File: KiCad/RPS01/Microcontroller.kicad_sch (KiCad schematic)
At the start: 20 parts, among them J1 Conn_02x03_Counter_Clockwise, J2 Conn_01x06, J3 Conn_01x03, J4 Conn_01x02_Pin, J5 XT30, J6 AandDpin, J7 Conn_01x03, SW1 MCU_Button, U1 ATmega328P-A, U2 AMS1117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

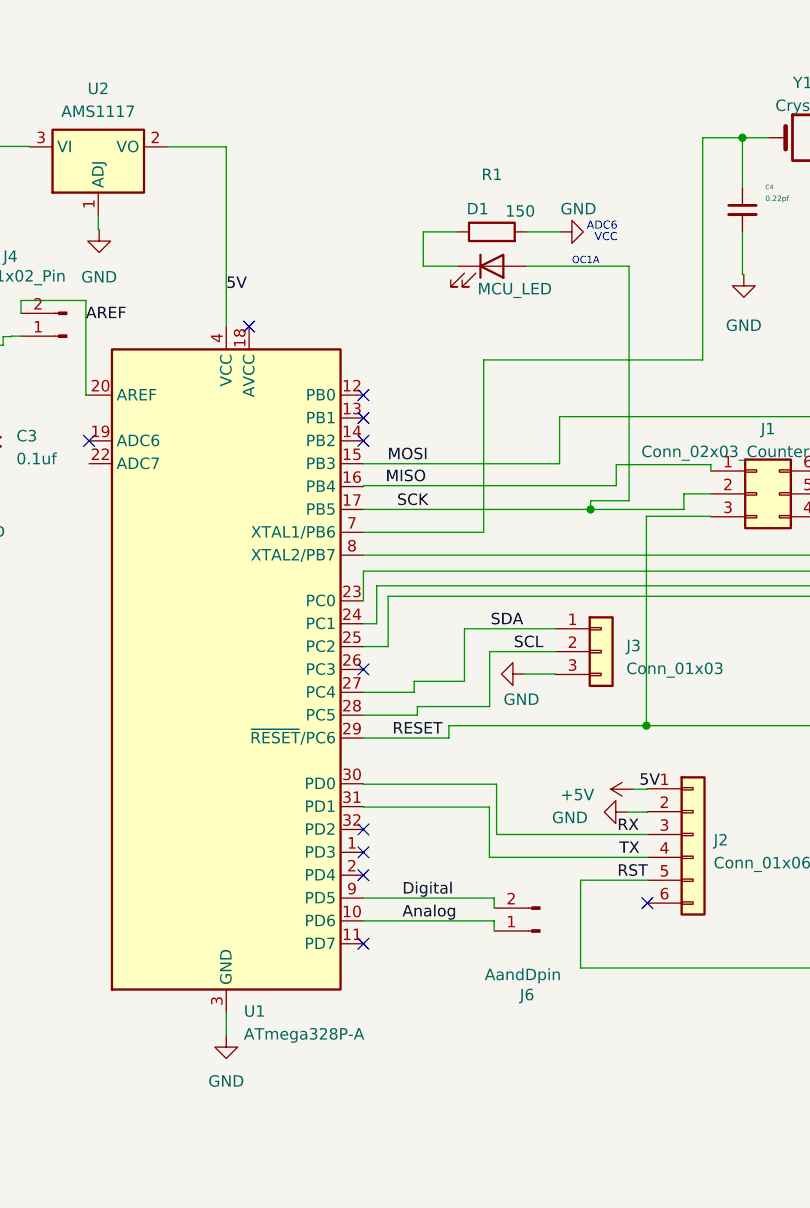
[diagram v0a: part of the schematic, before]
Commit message: 1206  to 0603
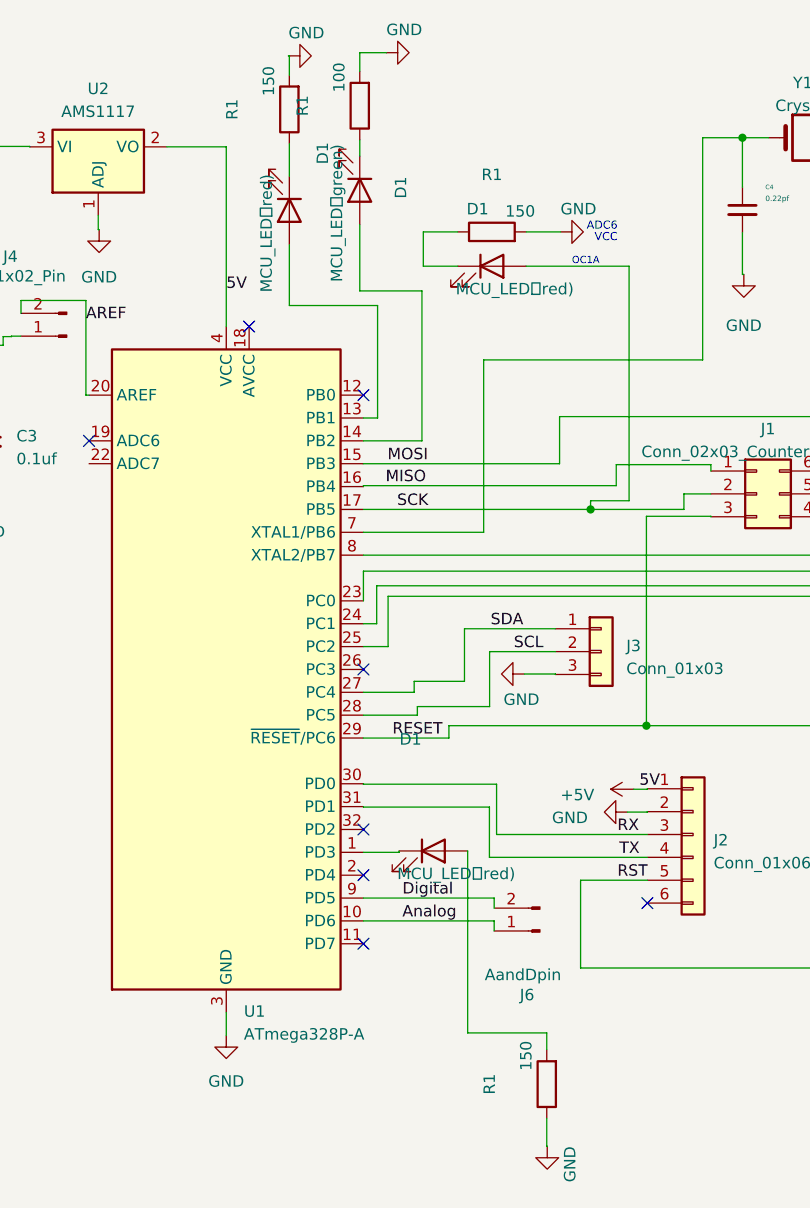
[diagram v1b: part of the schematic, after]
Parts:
- added D1: MCU_LED（green), LED_SMD:LED_RGB_5050-6, symbol Device:LED
- added D1 (x2): MCU_LED（red), LED_SMD:LED_RGB_5050-6, symbol Device:LED
- added R1: 100, Resistor_SMD:R_0603_1608Metric, symbol Device:R
- added R1 (x2): 150, Resistor_SMD:R_0603_1608Metric, symbol Device:R
- C1, C2, C3, C4, C5: footprint Capacitor_SMD:C_1206_3216Metric -> Capacitor_SMD:C_0603_1608Metric
- D1: value MCU_LED -> MCU_LED（red)
- R1, R4: footprint Resistor_SMD:R_1206_3216Metric -> Resistor_SMD:R_0603_1608Metric
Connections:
- net GND: now also R1.1, R1.2, R1.2
- net at U1.1 (PD3): now also D1.1 (K)
- net at U1.13 (PB1): now also D1.2 (A)
- net at U1.14 (PB2): now also D1.2 (A)
- new net: D1.1 (K), R1.1 (x2)
- new net: D1.2 (A), R1.2
- no-connect marks 13 -> 10

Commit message: RGB
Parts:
- removed D1: MCU_LED（green), LED_SMD:LED_RGB_5050-6, symbol Device:LED
- removed D1 (x3): MCU_LED（red), LED_SMD:LED_RGB_5050-6, symbol Device:LED
- removed R1: 150, Resistor_SMD:R_0603_1608Metric, symbol Device:R
- added J22: Conn_01x06_Pin, LED_SMD:LED_RGB_5050-6, symbol Connector:Conn_01x06_Pin
- R1: value 100 -> 100(red)
- R1: value 150 -> 150(blue)
- R1: value 150 -> 150(green)
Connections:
- net SCK is gone; now on net PD3: J1.2 (Pin_2), U1.17 (PB5)
- net GND: now also J22.4 (Pin_4), J22.5 (Pin_5), J22.6 (Pin_6); no longer R1.1, R1.2, R1.2
- net at R1.1: now also J22.1 (Pin_1)
- net PC2: now reaches J7.1 (Pin_1), U1.25 (PC2)
- net PC1: now reaches J7.2 (Pin_2), U1.24 (PC1)
- net PC0: now reaches J7.3 (Pin_3), U1.23 (PC0)
- net PB2: now reaches U1.14 (PB2)
- net PB2: now also R1.2
- net PD3: now reaches U1.1 (PD3)
- net PD3: now also R1.2
- net PB1: now reaches U1.13 (PB1)
- net PB1: now also R1.2
- net XTAL1: now reaches C4.1, U1.7 (XTAL1/PB6), Y1.1
- net XTAL2: now reaches C5.1, U1.8 (XTAL2/PB7), Y1.2
- net at R1.1: now also J22.2 (Pin_2)
- net Analog renamed PD6
- net Digital renamed PD5
- net VI renamed VIN
- new net: J22.3 (Pin_3), R1.1
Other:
- note removed: "ADC6"
- note removed: "OC1A"
- note removed: "VCC"
- moved on the sheet: R1

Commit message: 4.7K R
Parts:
- added R4 (x2): 4.7K, Resistor_SMD:R_0603_1608Metric, symbol Device:R
- J1: value Conn_02x03_Counter_Clockwise -> ISCP
- J2: value Conn_01x06 -> serial comm
- J3: value Conn_01x03 -> I2C pin
- J4: value Conn_01x02_Pin -> Aref
- J6: value AandDpin -> Temp
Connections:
- net GND: now also R4.1, R4.1
- net SCL: now also R4.2
- net SDA: now also R4.2
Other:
- moved on the sheet: J3

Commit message: updated MCU
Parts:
- J2: value serial comm -> Serial
- J22: value Conn_01x06_Pin -> RGB LED
- J3: value I2C pin -> i2c
- J6: value Temp -> Temperture
- J7: value Conn_01x03 -> GPIO
- Y1: value Crystal -> 16Mhz Crystal
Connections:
- no-connect marks 10 -> 11

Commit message: Large Schematic Update
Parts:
- removed J22: RGB LED, LED_SMD:LED_RGB_5050-6, symbol Connector:Conn_01x06_Pin
- removed J3: i2c, Connector_PinHeader_2.54mm:PinHeader_1x02_P2.54mm_Vertical_SMD_Pin1Right, symbol Connector_Generic:Conn_01x03
- removed J4: Aref, Connector_PinHeader_2.54mm:PinHeader_1x02_P2.54mm_Vertical_SMD_Pin1Left, symbol Connector:Conn_01x02_Pin
- removed J5: XT30, Connector_AMASS:AMASS_XT30U-F_1x02_P5.0mm_Vertical, symbol Connector:Conn_01x02_Pin
- removed J6: Temperture, Connector_PinHeader_2.54mm:PinHeader_1x02_P2.54mm_Vertical_SMD_Pin1Left, symbol Connector:Conn_01x02_Pin
- removed J7: GPIO, Connector_PinHeader_2.54mm:PinHeader_1x03_P2.54mm_Vertical_SMD_Pin1Left, symbol Connector_Generic:Conn_01x03
- removed R1: 100(red), Resistor_SMD:R_0603_1608Metric, symbol Device:R
- removed R1: 150(blue), Resistor_SMD:R_0603_1608Metric, symbol Device:R
- removed R1: 150(green), Resistor_SMD:R_0603_1608Metric, symbol Device:R
- removed R4 (x2): 4.7K, Resistor_SMD:R_0603_1608Metric, symbol Device:R
- removed U2: AMS1117, Package_TO_SOT_SMD:SOT-223-3_TabPin2, symbol Regulator_Linear:AMS1117
- added R11: 0, symbol Device:R_Small
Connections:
- net VIN is gone; now on net +5V: C2.1, U3.3 (VIN)
- net AREF: now also R11.2
- net PD3: no longer J1.2 (Pin_2), U1.17 (PB5)
- net PC3: now reaches U1.26 (PC3)
- net PD6: no longer names the net of U1.10 (PD6)
- net SCL renamed PC5
- net SDA renamed PC4
- net VOUT: no longer names the net of C3.1, U3.4 (VOUT)
- net VOUT: now also R11.1
- new net SCK: J1.2 (Pin_2), U1.17 (PB5)
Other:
- moved on the sheet: C3, J1, U3

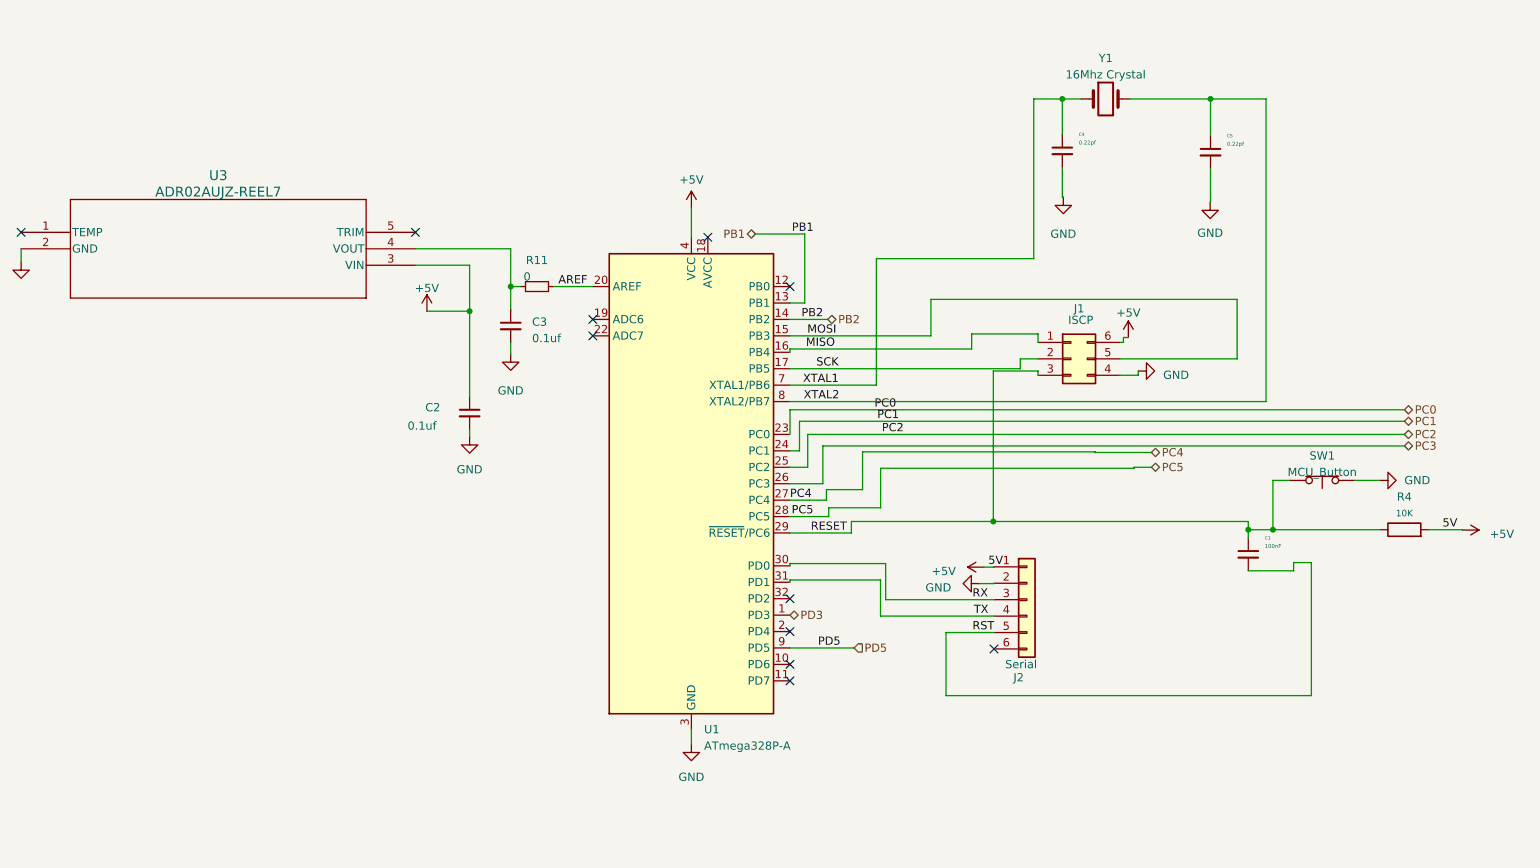
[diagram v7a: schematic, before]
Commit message: Finished most of the Schematics. Needs polishing
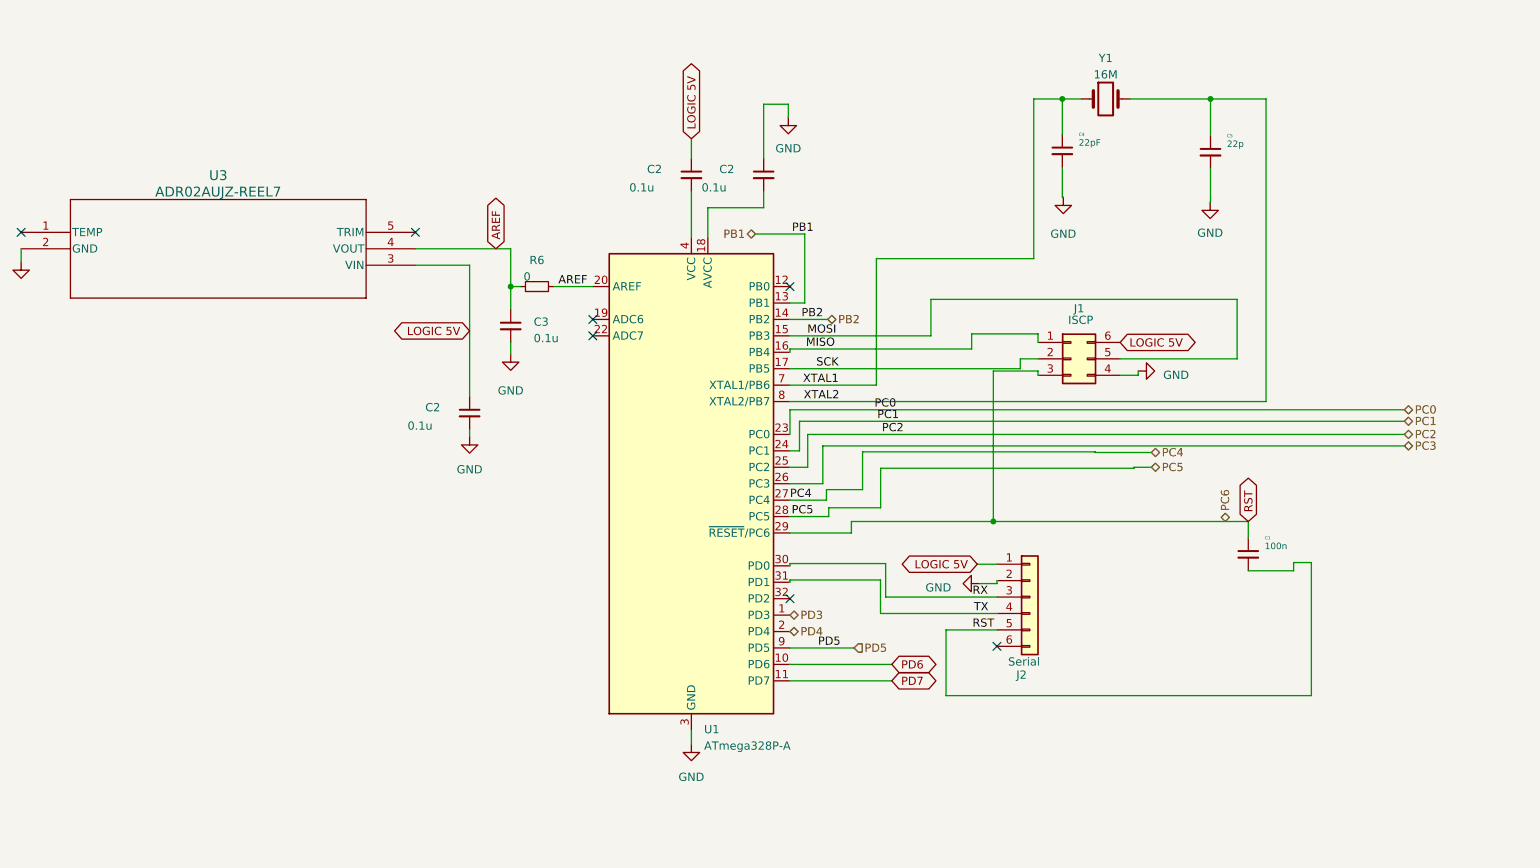
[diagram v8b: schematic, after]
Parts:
- removed R4: 10K, Resistor_SMD:R_0603_1608Metric, symbol Device:R
- removed SW1: MCU_Button, Button_Switch_SMD:SW_SPST_PTS645, symbol Switch:SW_Push_Open
- added C2 (x2): 0.1u, Capacitor_SMD:C_0603_1608Metric, symbol Device:C_Small
- C1: value 100nF -> 100n
- C2, C3: value 0.1uf -> 0.1u
- C4: value 0.22pf -> 22pF
- C5: value 0.22pf -> 22p
- Y1: value 16Mhz Crystal -> 16M
- renumbered R11 to R6
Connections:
- net RESET is gone; now on net RST: C1.1, J1.3 (Pin_3), U1.29 (~{RESET}/PC6)
- net AREF: now also C3.1, R6.1, U3.4 (VOUT)
- net GND: now also C2.1
- net PD6: now reaches U1.10 (PD6)
- net PD7: now reaches U1.11 (PD7)
- net at U1.18 (AVCC): now also C2.2
- net PD4: now reaches U1.2 (PD4)
- net +5V renamed LOGIC 5V
- net LOGIC 5V: now also C2.1; no longer U1.4 (VCC), U1.6 (VCC)
- new net: C2.2, U1.4 (VCC), U1.6 (VCC)
- no-connect marks 11 -> 7
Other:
- moved on the sheet: J2
